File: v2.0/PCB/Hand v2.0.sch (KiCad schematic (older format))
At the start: 35 parts, among them J1 Conn_ARM_JTAG_SWD_10, M1 Index_Servo, M2 Middle_Servo, M3 Ring_Servo, M4 Pinky_Servo, M5 Thumb_Servo, SW1 Power_Switch

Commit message: v2.0 fixed file naming issues
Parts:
- MYO1: symbol hand~parts:MyoWare -> Hand-v2.0-Parts:MyoWare
- REG2: symbol hand~parts:MIC2876-5.5YMT-TR -> Hand-v2.0-Parts:MIC2876-5.5YMT-TR
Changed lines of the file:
@@
 EESchema Schematic File Version 4
-LIBS:Hand Mark 2 Rev 1-cache
+LIBS:Hand v2.0-cache
 EELAYER 30 0
 EELAYER END
@@
 $EndComp
 $Comp
-L hand~parts:MyoWare MYO1
+L Hand-v2.0-Parts:MyoWare MYO1
 U 1 1 5E217809
 P 6400 4950
@@
 $EndComp
 $Comp
-L hand~parts:MIC2876-5.5YMT-TR REG2
+L Hand-v2.0-Parts:MIC2876-5.5YMT-TR REG2
 U 1 1 5E2A2729
 P 3800 5400

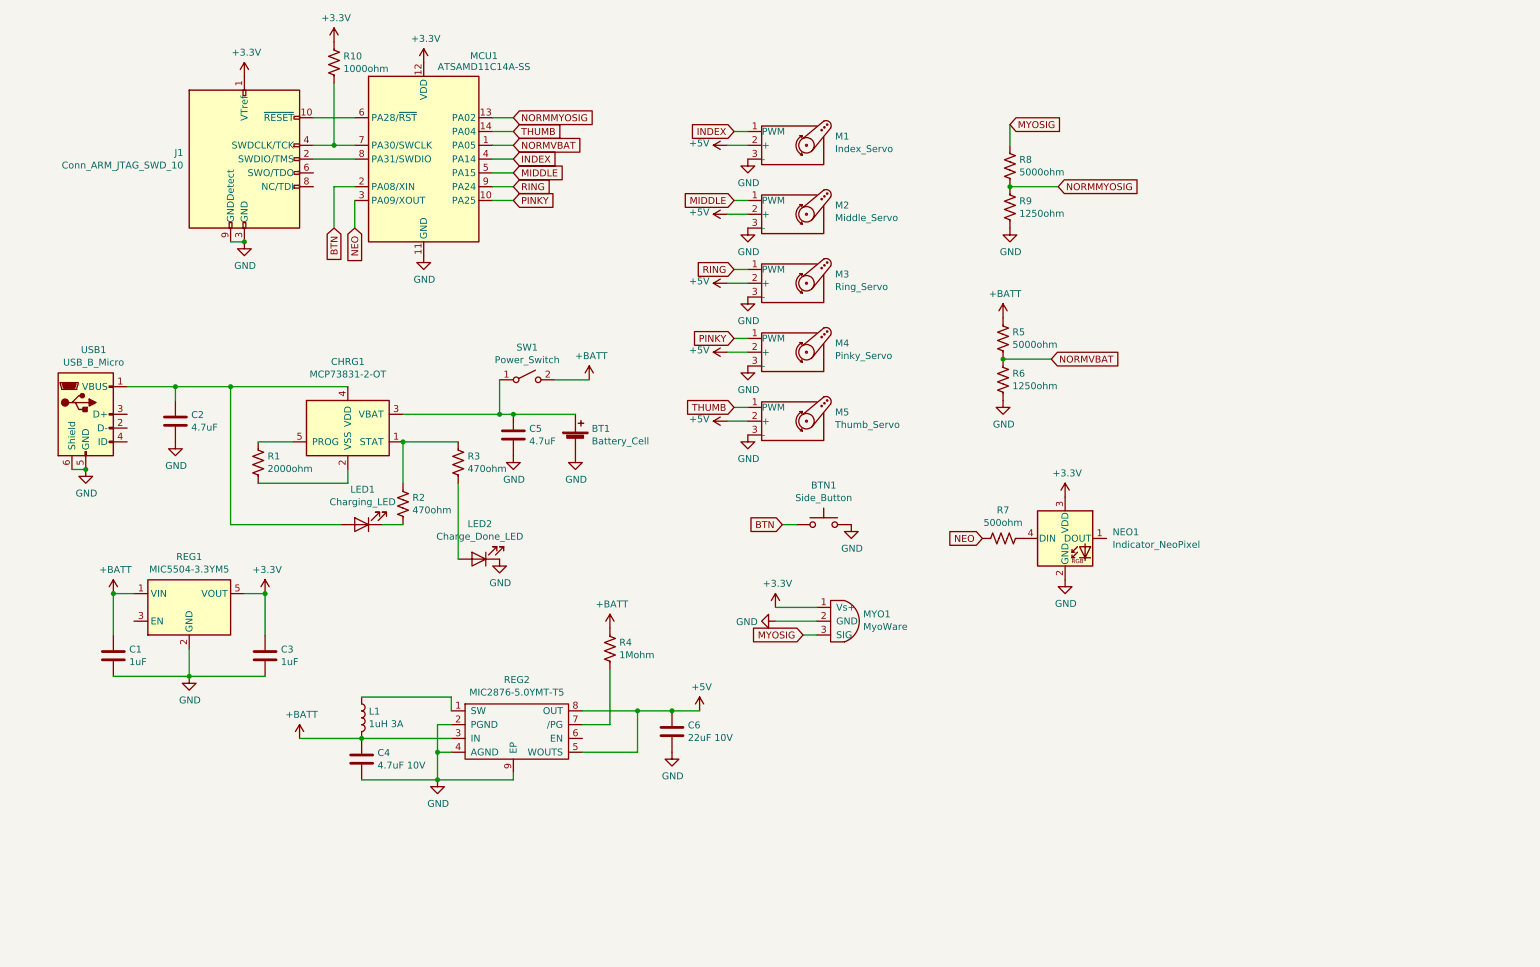
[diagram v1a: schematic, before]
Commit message: began swapping arm chips
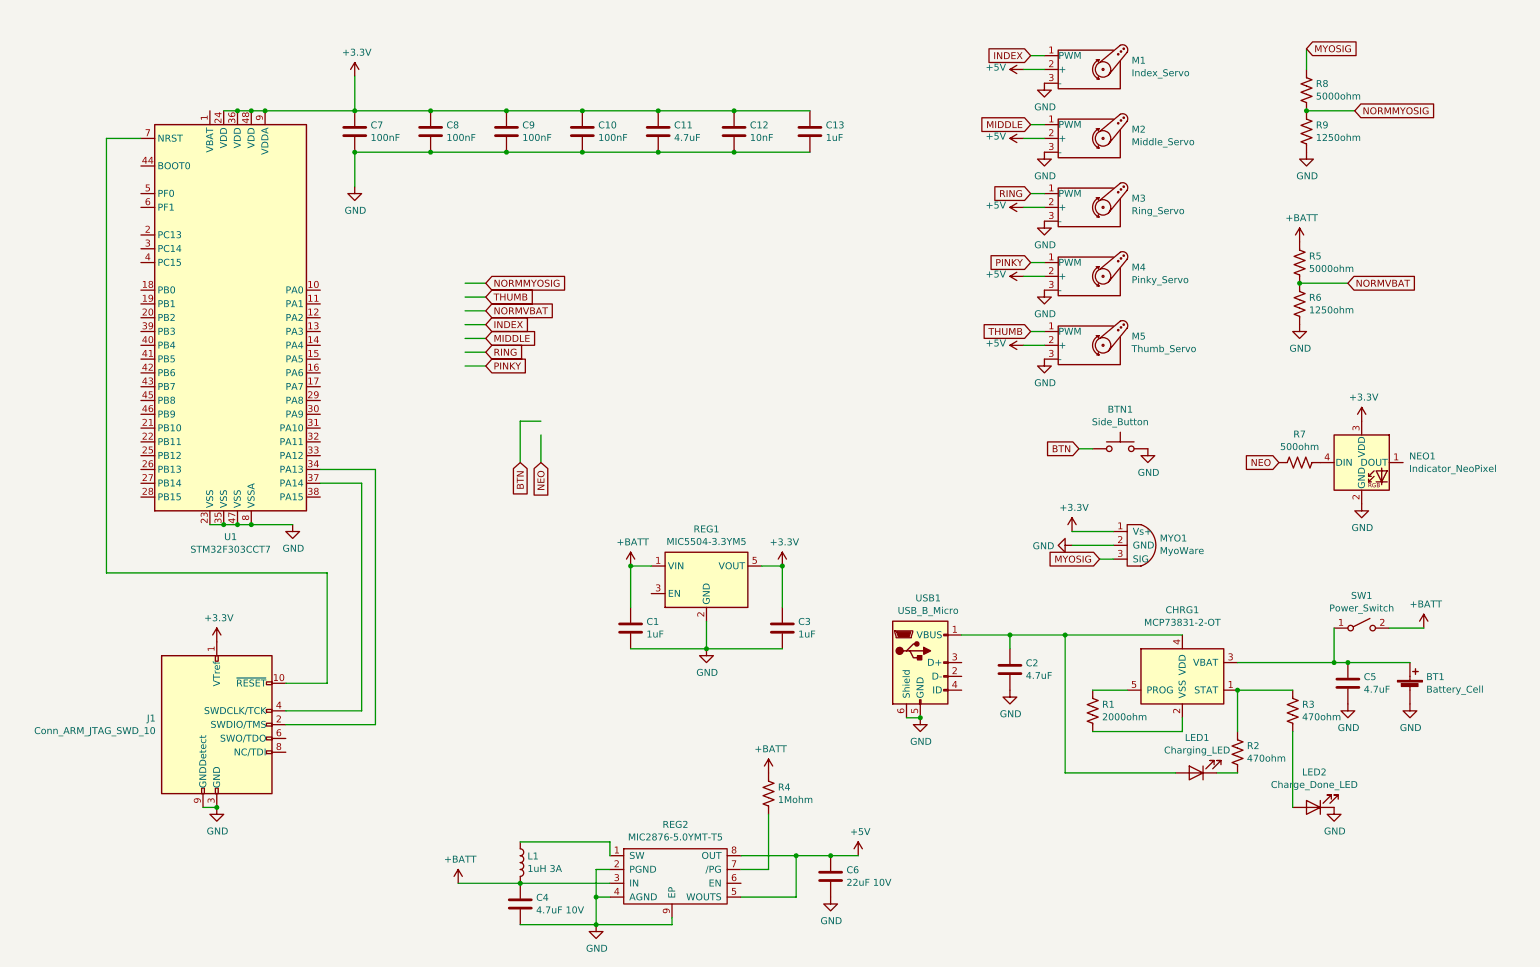
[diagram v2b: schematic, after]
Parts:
- removed MCU1: ATSAMD11C14A-SS, Package_SO:SOIC-14_3.9x8.7mm_P1.27mm, symbol MCU_Microchip_SAMD:ATSAMD11C14A-SS
- removed R10: 1000ohm, Resistor_SMD:R_0805_2012Metric_Pad1.15x1.40mm_HandSolder, symbol Device:R_US
- added C10, C7, C8, C9: 100nF, Capacitor_SMD:C_0805_2012Metric_Pad1.15x1.40mm_HandSolder, symbol Device:C
- added C11: 4.7uF, Capacitor_SMD:C_0805_2012Metric_Pad1.15x1.40mm_HandSolder, symbol Device:C
- added C12: 10nF, Capacitor_SMD:C_0805_2012Metric_Pad1.15x1.40mm_HandSolder, symbol Device:C
- added C13: 1uF, Capacitor_SMD:C_0805_2012Metric_Pad1.15x1.40mm_HandSolder, symbol Device:C
- added U1: STM32F303CCT7, Package_QFP:LQFP-48_7x7mm_P0.5mm, symbol MCU_ST_STM32F3:STM32F303CCTx
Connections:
- wire segments 77 -> 105
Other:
- moved on the sheet: BT1, BTN1, C1, C2, C3, C4, C5, C6, CHRG1, J1, L1, LED1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
